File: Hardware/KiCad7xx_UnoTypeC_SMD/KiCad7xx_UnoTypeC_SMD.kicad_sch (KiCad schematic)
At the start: 72 parts, among them J1 -, J2 PINHD-1X18, T1 FDN340P, U1 MC33269ST, U2 LP2985-XXDBVR, U3 ATMEGA16U2, U4 ATMEGAXX8-MUR, U5 LMV358?MM, X1 POWERSUPPLY_DC21MMX, X2 USB-B_TH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

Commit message: feat: 取り付け穴が消えてしまう為,新たにM3_IOS14580を追加
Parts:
- removed FRAME1: DNP, UNOSMD_V3:FRAME, symbol UNOSMD_V3-eagle-import:A3-FRAME-STANDARD
- added H1, H2, H3, H4: MountingHole, MountingHole:MountingHole_3.2mm_M3_ISO14580, symbol Mechanical:MountingHole

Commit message: feat: Type-Cコネクタの回路を追加
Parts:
- removed C11, C9: 22p, UNOSMD_V3:C0603-ROUND, symbol UNOSMD_V3-eagle-import:C-EU0603-RND
- removed X2: USB-B_TH, UNOSMD_V3:PN61729, symbol UNOSMD_V3-eagle-import:PN61729
- removed Y1: 16MHz, UNOSMD_V3:QS, symbol UNOSMD_V3-eagle-import:XTAL/S
- added J1: USB_C_Receptacle_USB2.0, Connector_USB:USB_C_Receptacle_HRO_TYPE-C-31-M-12, symbol Connector:USB_C_Receptacle_USB2.0
- added R3, R4: 5.1k, UNOSMD_V3:R0603-ROUND, symbol Device:R
- added Y1: RESONATORMU, UNOSMD_V3:RESONATOR, symbol UNOSMD_V3-eagle-import:RESONATORMU
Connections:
- net D+: now also J1.A6 (D+), J1.B6 (D+)
- net D-: now also J1.A7 (D-), J1.B7 (D-)
- net GND: now also R3.1, R4.1, Y1.2
- net UGND: now also J1.A1 (GND), J1.A12 (GND), J1.B1 (GND), J1.B12 (GND)
- net USHIELD: now also J1.S1 (SHIELD)
- net XT1: now also Y1.3
- net XT2: now also Y1.1
- net XUSB: now also J1.A4 (VBUS), J1.A9 (VBUS), J1.B4 (VBUS), J1.B9 (VBUS)
- new net: J1.B5 (CC2), R4.2
- new net: J1.A5 (CC1), R3.2
- no-connect marks 0 -> 2
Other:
- moved on the sheet: C1, C10, C2, C3, C4, C5, C6, C7, C8, D1, D2, D3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

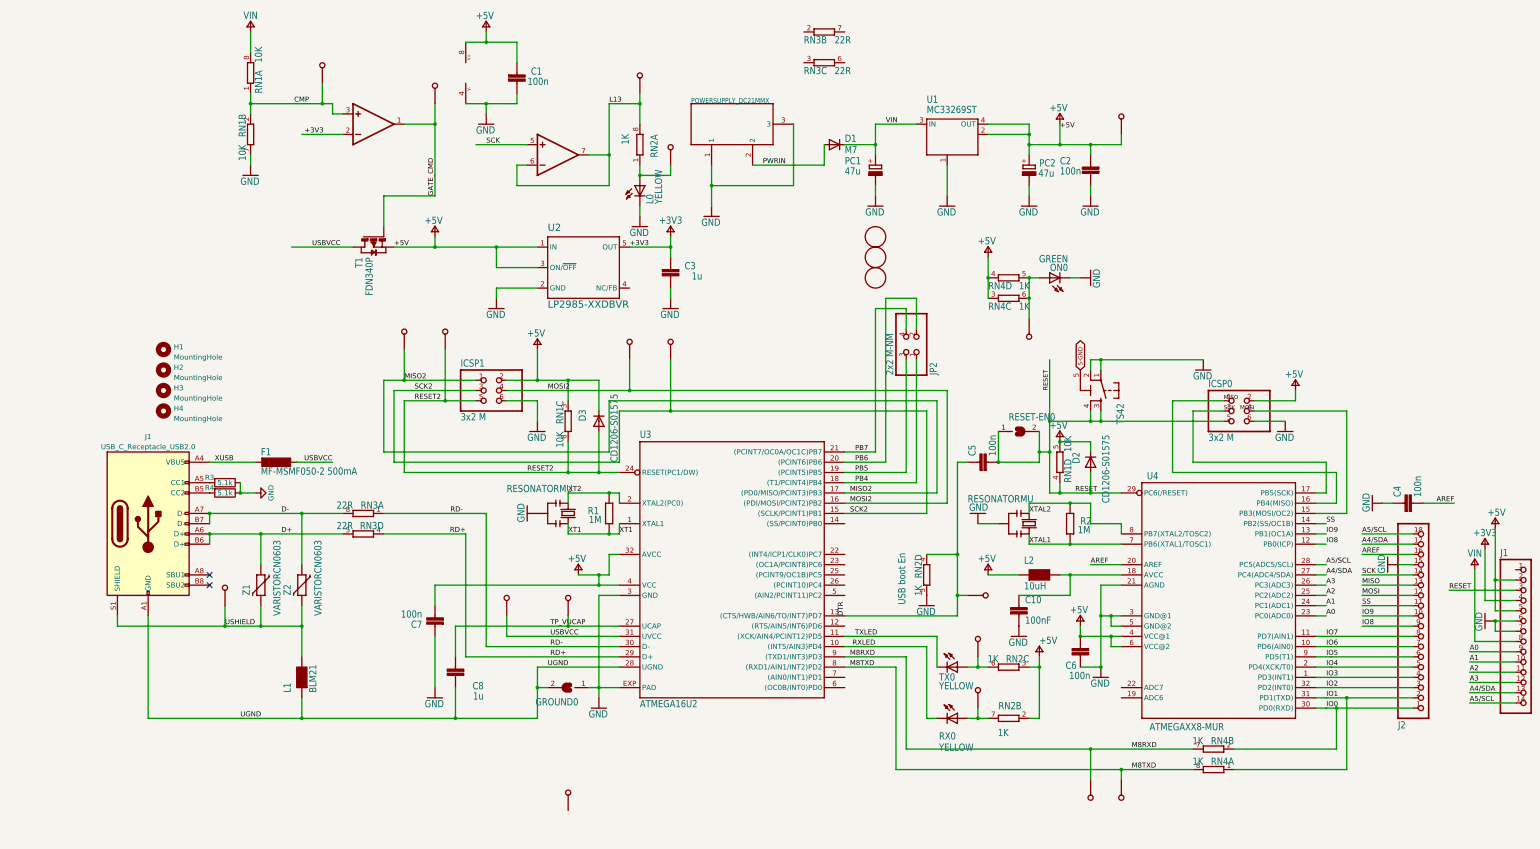
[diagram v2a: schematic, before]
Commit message: feat: 回路図を見やすくするために変更
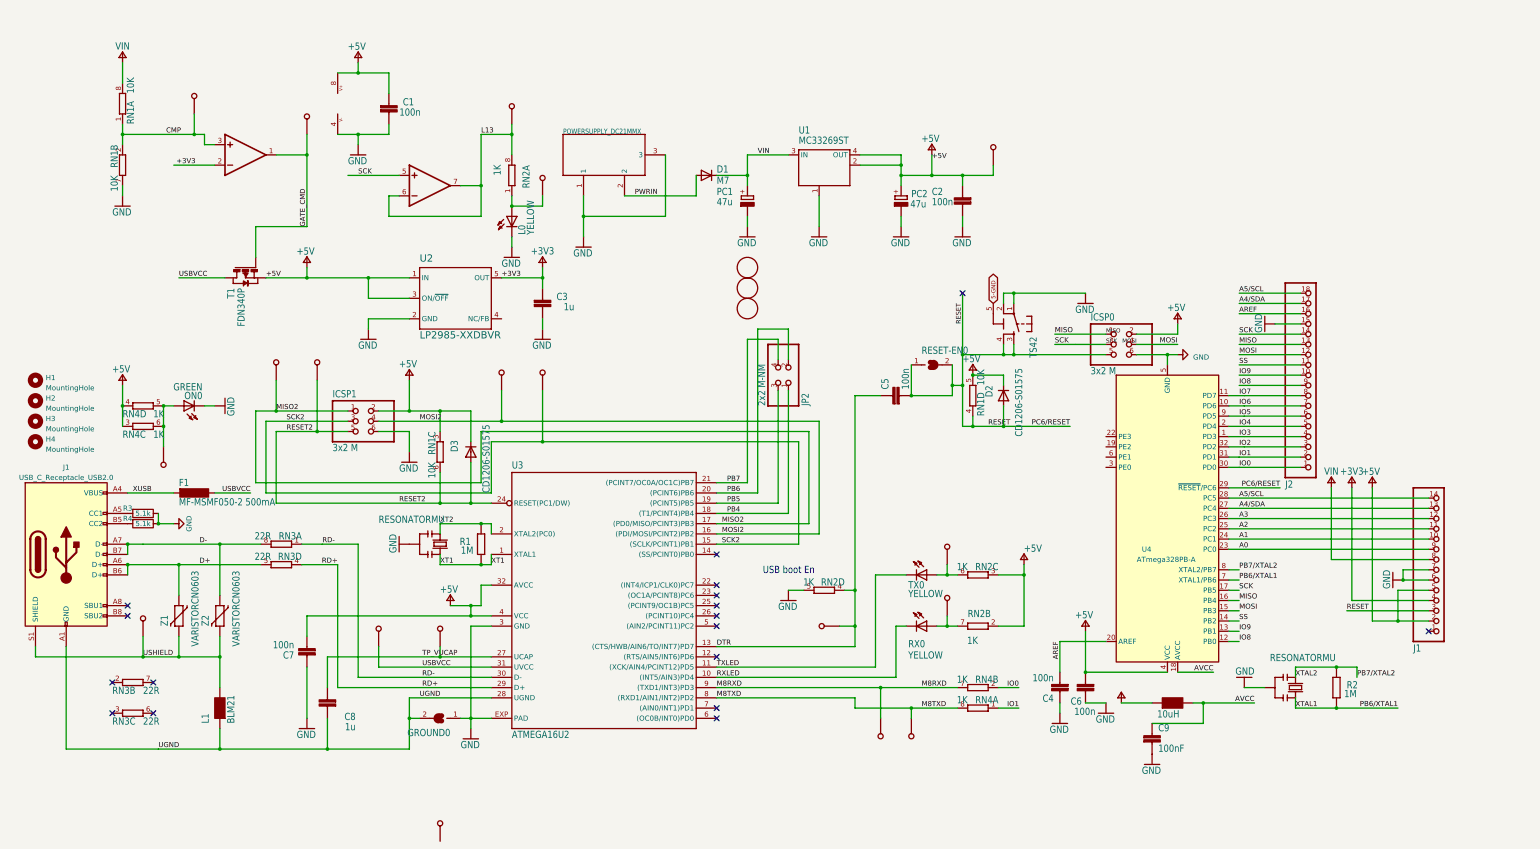
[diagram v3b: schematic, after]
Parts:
- removed C10: 100nF, UNOSMD_V3:C0603-ROUND, symbol UNOSMD_V3-eagle-import:0015_100NF_0603
- removed U4: ATMEGAXX8-MUR, UNOSMD_V3:MLF32, symbol UNOSMD_V3-eagle-import:ATMEGAXX8-MUR
- added C9: 100nF, UNOSMD_V3:C0603-ROUND, symbol UNOSMD_V3-eagle-import:0015_100NF_0603
- added U4: ATmega328PB-A, Package_QFP:TQFP-32_7x7mm_P0.8mm, symbol MCU_Microchip_ATmega:ATmega328PB-A
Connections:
- net +5V: now also U4.4 (VCC)
- net A0: now also U4.23 (PC0)
- net A1: now also U4.24 (PC1)
- net A2: now also U4.25 (PC2)
- net A3: now also U4.26 (PC3)
- net A4/SDA: now also U4.27 (PC4)
- net A5/SCL: now also U4.28 (PC5)
- net AREF: now also U4.20 (AREF)
- net GND: now also C9.2, U4.21 (GND), U4.5 (GND)
- net IO0: now also U4.30 (PD0)
- net IO1: now also U4.31 (PD1)
- net IO2: now also U4.32 (PD2)
- net IO3: now also U4.1 (PD3)
- net IO4: now also U4.2 (PD4)
- net IO5: now also U4.9 (PD5)
- net IO6: now also U4.10 (PD6)
- net IO7: now also U4.11 (PD7)
- net IO8: now also U4.12 (PB0)
- net IO9: now also U4.13 (PB1)
- net MISO: now also U4.16 (PB4)
- net MOSI: now also U4.15 (PB3)
- net SCK: now also U4.17 (PB5)
- net SS: now also U4.14 (PB2)
- net AVCC: now reaches L2.2
- net AVCC: now also C9.1, U4.18 (AVCC)
- net RESET renamed PC6/RESET
- net PC6/RESET: now also U4.29 (~{RESET}/PC6)
- net XTAL1 renamed PB6/XTAL1
- net PB6/XTAL1: now also U4.7 (XTAL1/PB6)
- net XTAL2 renamed PB7/XTAL2
- net PB7/XTAL2: now also U4.8 (XTAL2/PB7)
- no-connect marks 2 -> 17
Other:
- moved on the sheet: C1, C2, C3, C5, C7, C8, D1, D2, D3, F1, GROUND0, H1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
